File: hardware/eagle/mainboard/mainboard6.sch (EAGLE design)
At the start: 35 parts, among them Q101 16MHz

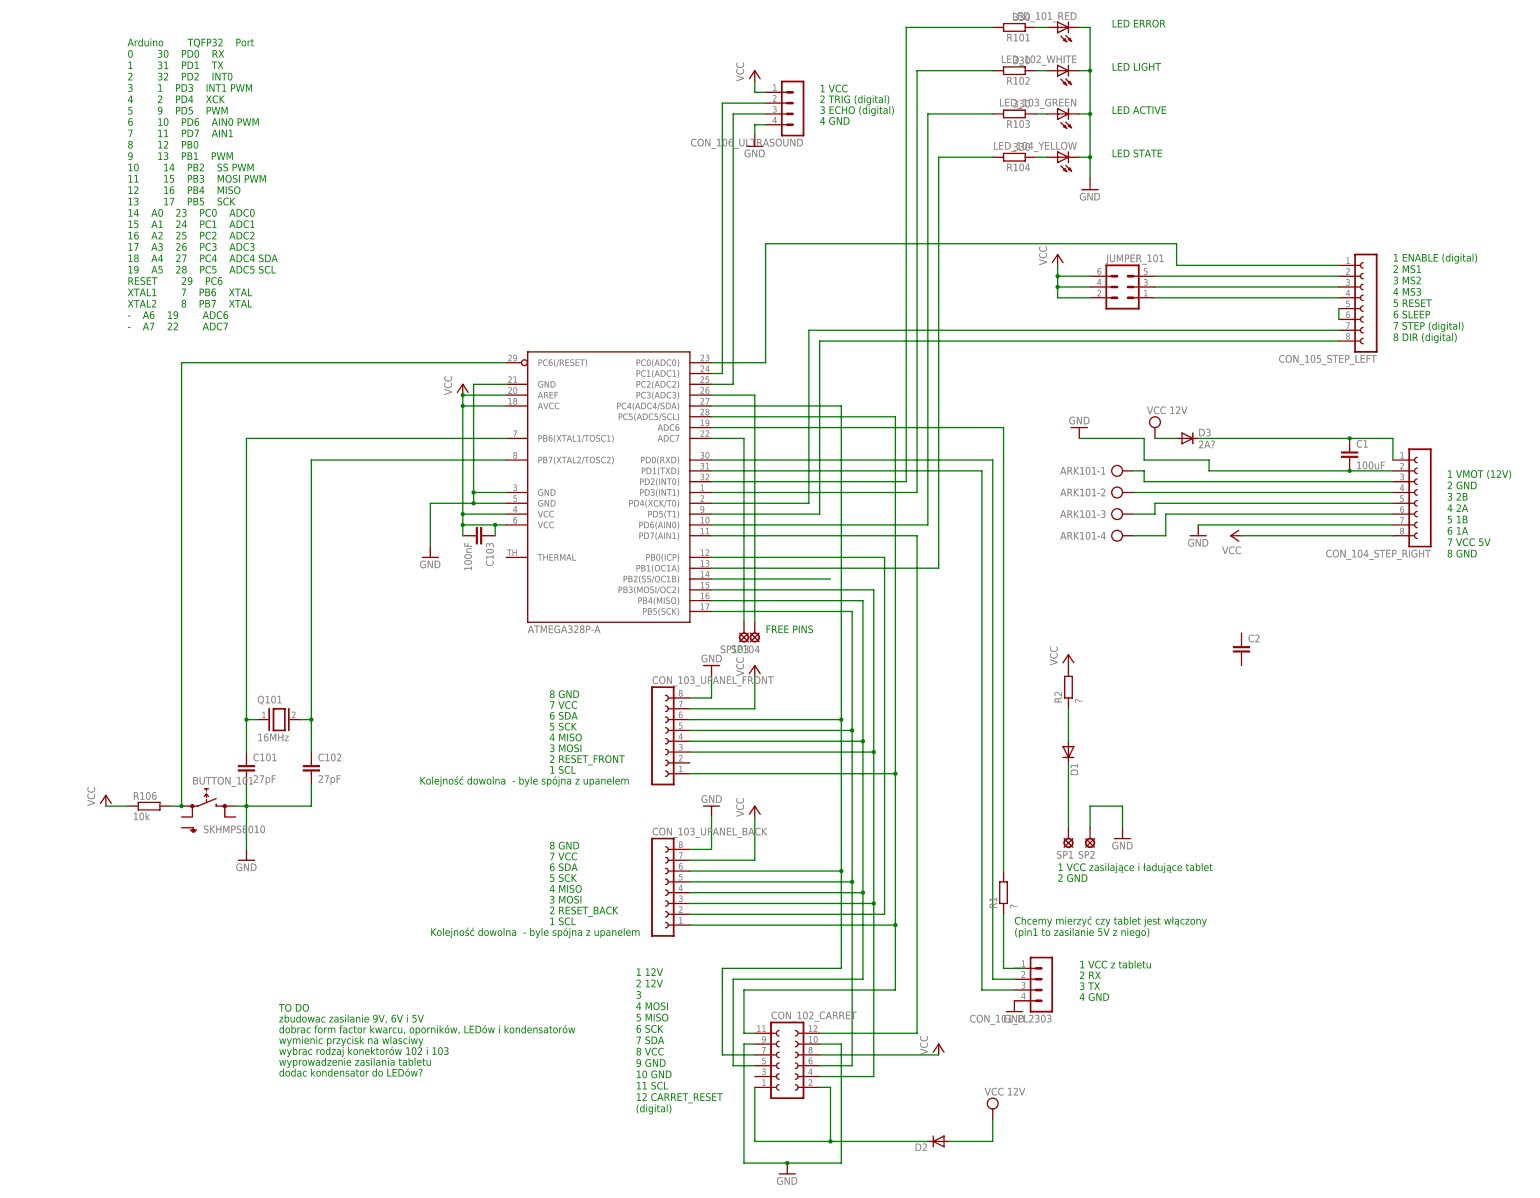
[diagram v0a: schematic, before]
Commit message: Cofniecie zmian z eagle 6
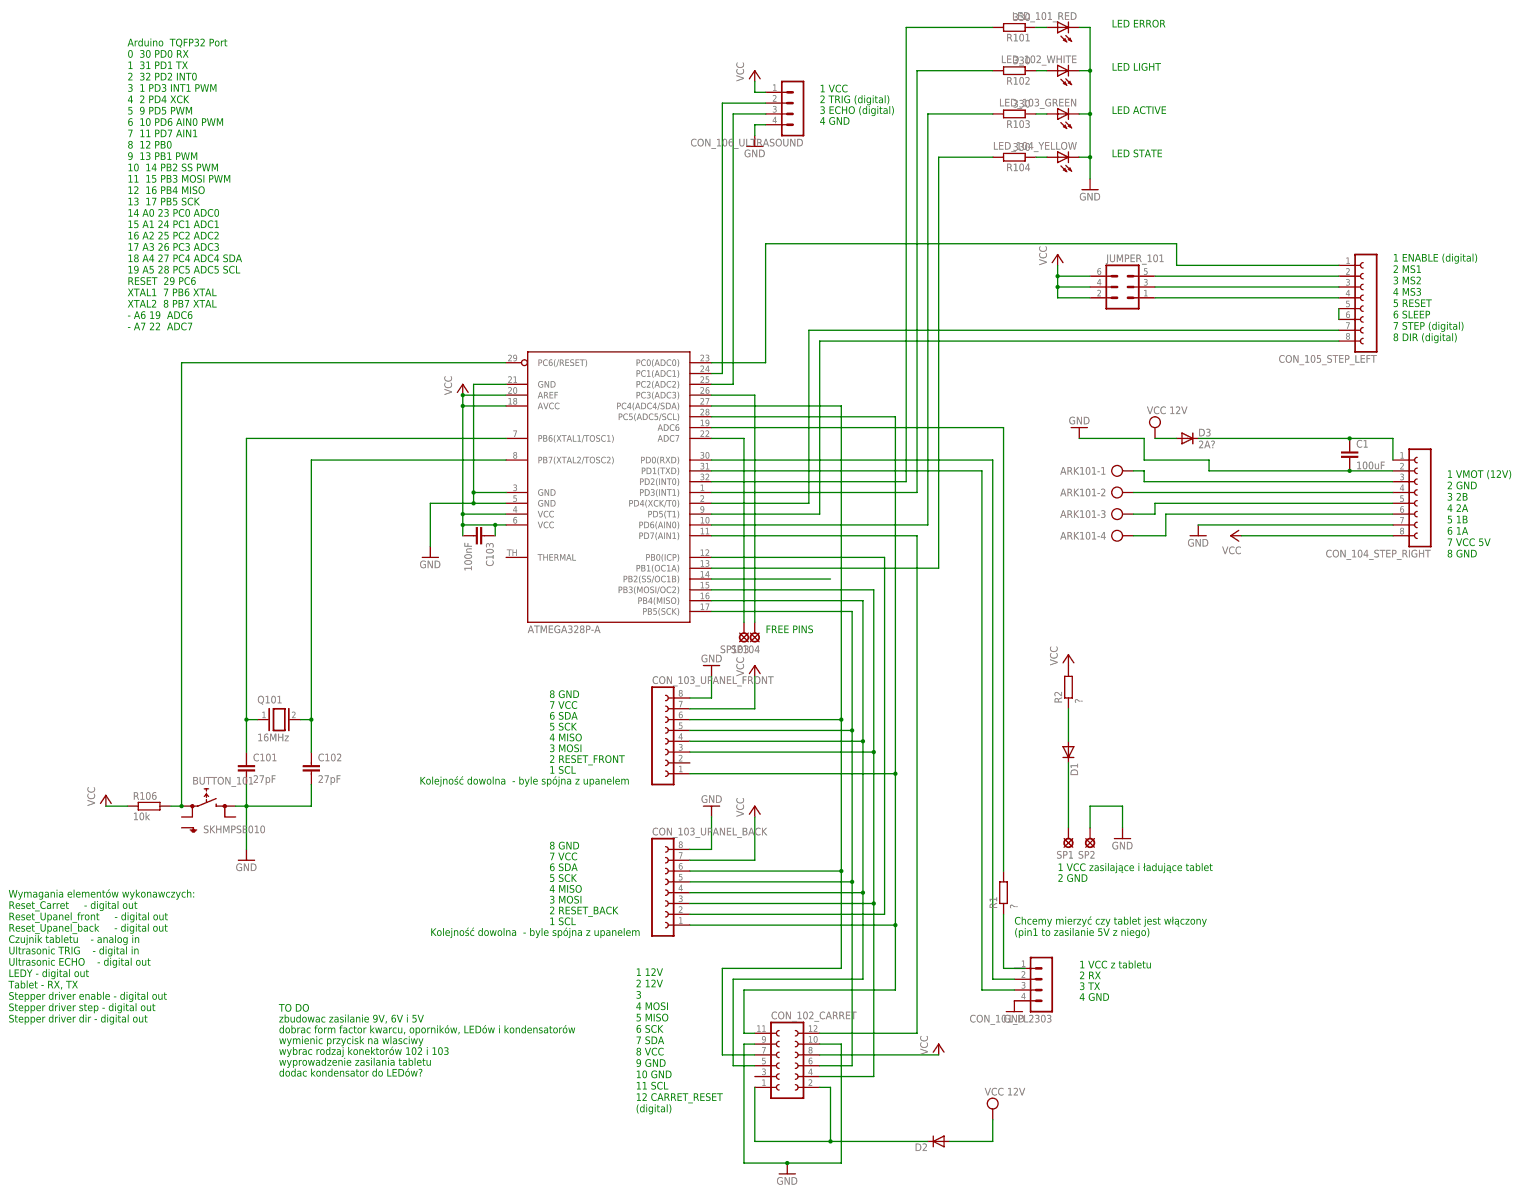
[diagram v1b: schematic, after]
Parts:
- removed C2: (no value), eagle-ltspice:C
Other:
- note added: "Wymagania elementów wykonawczych: Reset_Carret - digital out Reset_Upanel_front - digital out Reset_Upanel_back - digital out Czujnik tabletu - analog in Ultrasonic TRIG - digital in Ultrasonic ECHO - digital out LEDY - digital out Tablet - RX, TX Stepper driver enable - digital out Stepper driver step - digital out Stepper driver dir - digital out"
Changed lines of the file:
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@@
 <part name="D3" library="diode" deviceset="1N5060GP" device="" value="2A?"/>
 <part name="C1" library="eagle-ltspice" deviceset="C" device="" value="100uF"/>
-<part name="C2" library="eagle-ltspice" deviceset="C" device=""/>
 </parts>
 <sheets>
@@
 <text x="-83.82" y="-33.02" size="1.778" layer="91">Kolejność dowolna  - byle spójna z upanelem</text>
 <text x="-81.28" y="-68.58" size="1.778" layer="91">Kolejność dowolna  - byle spójna z upanelem</text>
-<text x="-152.4" y="73.66" size="1.778" layer="91" font="fixed">Arduino		TQFP32	Port
-0		30	PD0	RX
-1		31	PD1	TX
-2		32	PD2	INT0
-3		1	PD3	INT1 PWM
-4		2	PD4	XCK
-5		9	PD5	PWM
-6		10	PD6	AIN0 PWM
-7		11	PD7	AIN1
-8		12	PB0
-9		13	PB1	PWM
-10		14	PB2	SS PWM
-11		15	PB3	MOSI PWM
-12		16	PB4	MISO
-13		17	PB5	SCK
-14	A0	23	PC0	ADC0
-15	A1	24	PC1	ADC1
-16	A2	25	PC2	ADC2
-17	A3	26	PC3	ADC3
-18	A4	27	PC4	ADC4 SDA
-19	A5	28	PC5	ADC5 SCL
-RESET		29	PC6
-XTAL1		7	PB6	XTAL
-XTAL2		8	PB7	XTAL
--	A6	19		ADC6
--	A7	22		ADC7
+<text x="-152.4" y="73.66" size="1.778" layer="91" font="fixed">Arduino  TQFP32 Port
+0  30 PD0 RX
+1  31 PD1 TX
+2  32 PD2 INT0
+3  1 PD3 INT1 PWM
+4  2 PD4 XCK
+5  9 PD5 PWM
+6  10 PD6 AIN0 PWM
+7  11 PD7 AIN1
+8  12 PB0
+9  13 PB1 PWM
+10  14 PB2 SS PWM
+11  15 PB3 MOSI PWM
+12  16 PB4 MISO
+13  17 PB5 SCK
+14 A0 23 PC0 ADC0
+15 A1 24 PC1 ADC1
+16 A2 25 PC2 ADC2
+17 A3 26 PC3 ADC3
+18 A4 27 PC4 ADC4 SDA
+19 A5 28 PC5 ADC5 SCL
+RESET  29 PC6
+XTAL1  7 PB6 XTAL
+XTAL2  8 PB7 XTAL
+- A6 19  ADC6
+- A7 22  ADC7
 </text>
 <text x="144.78" y="71.12" size="1.778" layer="91">1 ENABLE (digital)
@@
 12 CARRET_RESET
 (digital)</text>
+<text x="-180.34" y="-88.9" size="1.778" layer="91">Wymagania elementów wykonawczych:
+Reset_Carret	 - digital out
+Reset_Upanel_front	 - digital out
+Reset_Upanel_back	 - digital out
+Czujnik tabletu	- analog in
+Ultrasonic TRIG	- digital in
+Ultrasonic ECHO	- digital out
+LEDY - digital out
+Tablet - RX, TX
+Stepper driver enable - digital out
+Stepper driver step - digital out
+Stepper driver dir - digital out</text>
 </plain>
 <instances>
@@
 <instance part="D3" gate="1" x="96.52" y="48.26"/>
 <instance part="C1" gate="G$1" x="134.62" y="45.72"/>
-<instance part="C2" gate="G$1" x="109.22" y="0"/>
 </instances>
 <busses>

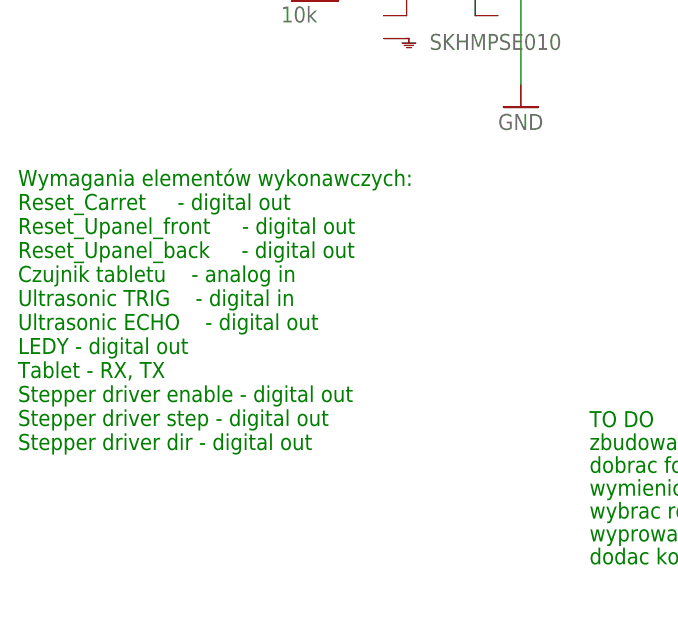
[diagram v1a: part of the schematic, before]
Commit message: Wstawienie diód i poprawki w zasilaniu
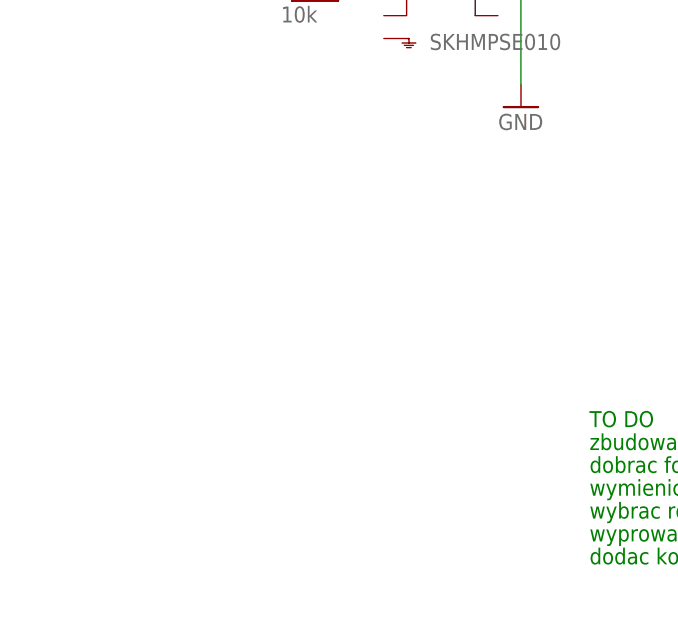
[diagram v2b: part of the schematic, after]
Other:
- note removed: "Wymagania elementów wykonawczych: Reset_Carret - digital out Reset_Upanel_front - digital out Reset_Upanel_back - digital out Czujnik tabletu - analog in Ultrasonic TRIG - digital in Ultrasonic ECHO - digital out LEDY - digital out Tablet - RX, TX Stepper driver enable - digital out Stepper driver step - digital out Stepper driver dir - digital out"
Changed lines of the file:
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@@
 12 CARRET_RESET
 (digital)</text>
-<text x="-180.34" y="-88.9" size="1.778" layer="91">Wymagania elementów wykonawczych:
-Reset_Carret	 - digital out
-Reset_Upanel_front	 - digital out
-Reset_Upanel_back	 - digital out
-Czujnik tabletu	- analog in
-Ultrasonic TRIG	- digital in
-Ultrasonic ECHO	- digital out
-LEDY - digital out
-Tablet - RX, TX
-Stepper driver enable - digital out
-Stepper driver step - digital out
-Stepper driver dir - digital out</text>
 </plain>
 <instances>
